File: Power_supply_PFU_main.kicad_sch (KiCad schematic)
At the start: 0 parts

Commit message: ahora modifique dos sch
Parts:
- added U1: ADA4610-4xR, Package_SO:SOIC-14_3.9x8.7mm_P1.27mm, symbol Amplifier_Operational:ADA4610-4xR
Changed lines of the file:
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@@
 		(dnp no)
 		(fields_autoplaced yes)
-		(property "Reference" "#PWR01"
+		(property "Reference" "#PWR?"
 			(at 38.1 41.91 0)
 			(effects
@@
 		)
 		(instances
+			(project "Power_supply_PFU_main"
+				(path "/82539c6a-c35d-43cd-a39f-64e847c1536b"
+					(reference "#PWR?")
+					(unit 1)
+				)
+			)
 			(project "HW_HTB_PFU_MAIN"
 				(path "/8502ea7d-f2d8-4443-99aa-8c64d27b64f2/8af84ec4-f9ff-4e86-b3d8-160fe4617c9c"
@@
 		(dnp no)
 		(fields_autoplaced yes)
-		(property "Reference" "#PWR05"
+		(property "Reference" "#PWR?"
 			(at 59.69 27.94 0)
 			(effects
@@
 		)
 		(instances
+			(project "Power_supply_PFU_main"
+				(path "/82539c6a-c35d-43cd-a39f-64e847c1536b"
+					(reference "#PWR?")
+					(unit 1)
+				)
+			)
 			(project "HW_HTB_PFU_MAIN"
 				(path "/8502ea7d-f2d8-4443-99aa-8c64d27b64f2/8af84ec4-f9ff-4e86-b3d8-160fe4617c9c"
@@
 		(dnp no)
 		(fields_autoplaced yes)
-		(property "Reference" "#PWR04"
+		(property "Reference" "#PWR?"
 			(at 59.69 31.75 0)
 			(effects
@@
 		)
 		(instances
+			(project "Power_supply_PFU_main"
+				(path "/82539c6a-c35d-43cd-a39f-64e847c1536b"
+					(reference "#PWR?")
+					(unit 1)
+				)
+			)
 			(project "HW_HTB_PFU_MAIN"
 				(path "/8502ea7d-f2d8-4443-99aa-8c64d27b64f2/8af84ec4-f9ff-4e86-b3d8-160fe4617c9c"
 					(reference "#PWR04")
+					(unit 1)
+				)
+			)
+		)
+	)
+	(symbol
+		(lib_id "Amplifier_Operational:ADA4610-4xR")
+		(at 191.77 82.55 0)
+		(unit 1)
+		(exclude_from_sim no)
+		(in_bom yes)
+		(on_board yes)
+		(dnp no)
+		(fields_autoplaced yes)
+		(property "Reference" "U1"
+			(at 191.77 72.39 0)
+			(effects
+				(font
+					(size 1.27 1.27)
+				)
+			)
+		)
+		(property "Value" "ADA4610-4xR"
+			(at 191.77 74.93 0)
+			(effects
+				(font
+					(size 1.27 1.27)
+				)
+			)
+		)
+		(property "Footprint" "Package_SO:SOIC-14_3.9x8.7mm_P1.27mm"
+			(at 191.77 82.55 0)
+			(effects
+				(font
+					(size 1.27 1.27)
+				)
+				(hide yes)
+			)
+		)
+		(property "Datasheet" "https://www.analog.com/media/en/technical-documentation/data-sheets/ADA4610-1_4610-2_4610-4.pdf"
+			(at 191.77 82.55 0)
+			(effects
+				(font
+					(size 1.27 1.27)
+				)
+				(hide yes)
+			)
+		)
+		(property "Description" "Quad Low Noise, Precision, Rail-to-Rail Output, JFET Single Op Amp, SOIC-14"
+			(at 191.77 82.55 0)
+			(effects
+				(font
+					(size 1.27 1.27)
+				)
+				(hide yes)
+			)
+		)
+		(pin "2"
+		)
+		(pin "3"
+		)
+		(pin "1"
+		)
+		(pin "5"
+		)
+		(pin "6"
+		)
+		(pin "7"
+		)
+		(pin "10"
+		)
+		(pin "8"
+		)
+		(pin "12"
+		)
+		(pin "13"
+		)
+		(pin "14"
+		)
+		(pin "9"
+		)
+		(pin "4"
+		)
+		(pin "11"
+		)
+		(instances
+			(project ""
+				(path "/82539c6a-c35d-43cd-a39f-64e847c1536b"
+					(reference "U1")
 					(unit 1)
 				)
@@
 		(dnp no)
 		(fields_autoplaced yes)
-		(property "Reference" "#PWR02"
+		(property "Reference" "#PWR?"
 			(at 54.61 43.18 0)
 			(effects
@@
 		)
 		(instances
+			(project "Power_supply_PFU_main"
+				(path "/82539c6a-c35d-43cd-a39f-64e847c1536b"
+					(reference "#PWR?")
+					(unit 1)
+				)
+			)
 			(project "HW_HTB_PFU_MAIN"
 				(path "/8502ea7d-f2d8-4443-99aa-8c64d27b64f2/8af84ec4-f9ff-4e86-b3d8-160fe4617c9c"
@@
 		)
 	)
+	(sheet_instances
+		(path "/"
+			(page "1")
+		)
+	)
+	(embedded_fonts no)
 )

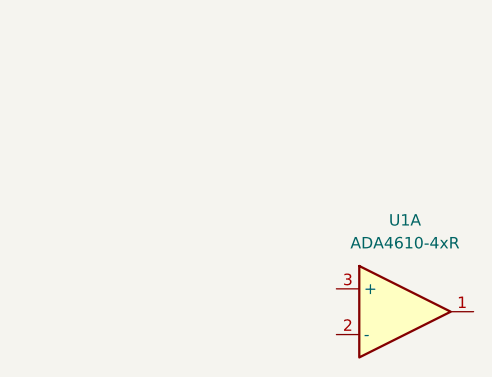
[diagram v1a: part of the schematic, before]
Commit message: Revert "ahora modifique dos sch"
This reverts commit 6d1ee52be01612af9494df4d4ac0ee7ca94c663e.
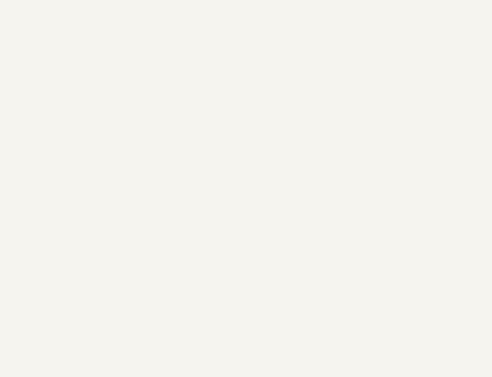
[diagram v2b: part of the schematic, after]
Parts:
- removed U1: ADA4610-4xR, Package_SO:SOIC-14_3.9x8.7mm_P1.27mm, symbol Amplifier_Operational:ADA4610-4xR
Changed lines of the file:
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@@
 		(dnp no)
 		(fields_autoplaced yes)
-		(property "Reference" "#PWR?"
+		(property "Reference" "#PWR01"
 			(at 38.1 41.91 0)
 			(effects
@@
 		)
 		(instances
-			(project "Power_supply_PFU_main"
-				(path "/82539c6a-c35d-43cd-a39f-64e847c1536b"
-					(reference "#PWR?")
-					(unit 1)
-				)
-			)
 			(project "HW_HTB_PFU_MAIN"
 				(path "/8502ea7d-f2d8-4443-99aa-8c64d27b64f2/8af84ec4-f9ff-4e86-b3d8-160fe4617c9c"
@@
 		(dnp no)
 		(fields_autoplaced yes)
-		(property "Reference" "#PWR?"
+		(property "Reference" "#PWR05"
 			(at 59.69 27.94 0)
 			(effects
@@
 		)
 		(instances
-			(project "Power_supply_PFU_main"
-				(path "/82539c6a-c35d-43cd-a39f-64e847c1536b"
-					(reference "#PWR?")
-					(unit 1)
-				)
-			)
 			(project "HW_HTB_PFU_MAIN"
 				(path "/8502ea7d-f2d8-4443-99aa-8c64d27b64f2/8af84ec4-f9ff-4e86-b3d8-160fe4617c9c"
@@
 		(dnp no)
 		(fields_autoplaced yes)
-		(property "Reference" "#PWR?"
+		(property "Reference" "#PWR04"
 			(at 59.69 31.75 0)
 			(effects
@@
 		)
 		(instances
-			(project "Power_supply_PFU_main"
-				(path "/82539c6a-c35d-43cd-a39f-64e847c1536b"
-					(reference "#PWR?")
-					(unit 1)
-				)
-			)
 			(project "HW_HTB_PFU_MAIN"
 				(path "/8502ea7d-f2d8-4443-99aa-8c64d27b64f2/8af84ec4-f9ff-4e86-b3d8-160fe4617c9c"
 					(reference "#PWR04")
-					(unit 1)
-				)
-			)
-		)
-	)
-	(symbol
-		(lib_id "Amplifier_Operational:ADA4610-4xR")
-		(at 191.77 82.55 0)
-		(unit 1)
-		(exclude_from_sim no)
-		(in_bom yes)
-		(on_board yes)
-		(dnp no)
-		(fields_autoplaced yes)
-		(property "Reference" "U1"
-			(at 191.77 72.39 0)
-			(effects
-				(font
-					(size 1.27 1.27)
-				)
-			)
-		)
-		(property "Value" "ADA4610-4xR"
-			(at 191.77 74.93 0)
-			(effects
-				(font
-					(size 1.27 1.27)
-				)
-			)
-		)
-		(property "Footprint" "Package_SO:SOIC-14_3.9x8.7mm_P1.27mm"
-			(at 191.77 82.55 0)
-			(effects
-				(font
-					(size 1.27 1.27)
-				)
-				(hide yes)
-			)
-		)
-		(property "Datasheet" "https://www.analog.com/media/en/technical-documentation/data-sheets/ADA4610-1_4610-2_4610-4.pdf"
-			(at 191.77 82.55 0)
-			(effects
-				(font
-					(size 1.27 1.27)
-				)
-				(hide yes)
-			)
-		)
-		(property "Description" "Quad Low Noise, Precision, Rail-to-Rail Output, JFET Single Op Amp, SOIC-14"
-			(at 191.77 82.55 0)
-			(effects
-				(font
-					(size 1.27 1.27)
-				)
-				(hide yes)
-			)
-		)
-		(pin "2"
-		)
-		(pin "3"
-		)
-		(pin "1"
-		)
-		(pin "5"
-		)
-		(pin "6"
-		)
-		(pin "7"
-		)
-		(pin "10"
-		)
-		(pin "8"
-		)
-		(pin "12"
-		)
-		(pin "13"
-		)
-		(pin "14"
-		)
-		(pin "9"
-		)
-		(pin "4"
-		)
-		(pin "11"
-		)
-		(instances
-			(project ""
-				(path "/82539c6a-c35d-43cd-a39f-64e847c1536b"
-					(reference "U1")
 					(unit 1)
 				)
@@
 		(dnp no)
 		(fields_autoplaced yes)
-		(property "Reference" "#PWR?"
+		(property "Reference" "#PWR02"
 			(at 54.61 43.18 0)
 			(effects
@@
 		)
 		(instances
-			(project "Power_supply_PFU_main"
-				(path "/82539c6a-c35d-43cd-a39f-64e847c1536b"
-					(reference "#PWR?")
-					(unit 1)
-				)
-			)
 			(project "HW_HTB_PFU_MAIN"
 				(path "/8502ea7d-f2d8-4443-99aa-8c64d27b64f2/8af84ec4-f9ff-4e86-b3d8-160fe4617c9c"
@@
 		)
 	)
-	(sheet_instances
-		(path "/"
-			(page "1")
-		)
-	)
-	(embedded_fonts no)
 )

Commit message: Modifico dos sch otra vez
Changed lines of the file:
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@@
+	(wire
+		(pts
+			(xy 138.43 99.06) (xy 138.43 73.66)
+		)
+		(stroke
+			(width 0)
+			(type default)
+		)
+	)
 	(wire
 		(pts
@@
 	(wire
 		(pts
+			(xy 67.31 99.06) (xy 138.43 99.06)
+		)
+		(stroke
+			(width 0)
+			(type default)
+		)
+	)
+	(wire
+		(pts
 			(xy 34.29 31.75) (xy 33.02 31.75)
+		)
+		(stroke
+			(width 0)
+			(type default)
+		)
+	)
+	(wire
+		(pts
+			(xy 138.43 73.66) (xy 171.45 73.66)
 		)
 		(stroke
@@
 		(dnp no)
 		(fields_autoplaced yes)
-		(property "Reference" "#PWR01"
+		(property "Reference" "#PWR?"
 			(at 38.1 41.91 0)
 			(effects
@@
 		)
 		(instances
+			(project "Power_supply_PFU_main"
+				(path "/82539c6a-c35d-43cd-a39f-64e847c1536b"
+					(reference "#PWR?")
+					(unit 1)
+				)
+			)
 			(project "HW_HTB_PFU_MAIN"
 				(path "/8502ea7d-f2d8-4443-99aa-8c64d27b64f2/8af84ec4-f9ff-4e86-b3d8-160fe4617c9c"
@@
 		(dnp no)
 		(fields_autoplaced yes)
-		(property "Reference" "#PWR05"
+		(property "Reference" "#PWR?"
 			(at 59.69 27.94 0)
 			(effects
@@
 		)
 		(instances
+			(project "Power_supply_PFU_main"
+				(path "/82539c6a-c35d-43cd-a39f-64e847c1536b"
+					(reference "#PWR?")
+					(unit 1)
+				)
+			)
 			(project "HW_HTB_PFU_MAIN"
 				(path "/8502ea7d-f2d8-4443-99aa-8c64d27b64f2/8af84ec4-f9ff-4e86-b3d8-160fe4617c9c"
@@
 		(dnp no)
 		(fields_autoplaced yes)
-		(property "Reference" "#PWR04"
+		(property "Reference" "#PWR?"
 			(at 59.69 31.75 0)
 			(effects
@@
 		)
 		(instances
+			(project "Power_supply_PFU_main"
+				(path "/82539c6a-c35d-43cd-a39f-64e847c1536b"
+					(reference "#PWR?")
+					(unit 1)
+				)
+			)
 			(project "HW_HTB_PFU_MAIN"
 				(path "/8502ea7d-f2d8-4443-99aa-8c64d27b64f2/8af84ec4-f9ff-4e86-b3d8-160fe4617c9c"
@@
 		(dnp no)
 		(fields_autoplaced yes)
-		(property "Reference" "#PWR02"
+		(property "Reference" "#PWR?"
 			(at 54.61 43.18 0)
 			(effects
@@
 		)
 		(instances
+			(project "Power_supply_PFU_main"
+				(path "/82539c6a-c35d-43cd-a39f-64e847c1536b"
+					(reference "#PWR?")
+					(unit 1)
+				)
+			)
 			(project "HW_HTB_PFU_MAIN"
 				(path "/8502ea7d-f2d8-4443-99aa-8c64d27b64f2/8af84ec4-f9ff-4e86-b3d8-160fe4617c9c"
@@
 		)
 	)
+	(sheet_instances
+		(path "/"
+			(page "1")
+		)
+	)
+	(embedded_fonts no)
 )
